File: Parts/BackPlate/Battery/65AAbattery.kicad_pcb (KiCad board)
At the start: 2 copper layers, 172.9 x 20 mm, 10 parts, among them J1 Conn_01x02, J2 Conn_01x01, J3 Conn_01x01, J4 Conn_01x01, SW1 SW_Push_SPDT

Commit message: 寸法更新とか
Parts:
- J1: footprint kbd_Parts:Battery_XH2.5_GL_rev -> kbd_Parts:Battery_XH2.5_GL_Connector
- moved C1 9.45 mm to (148.8, 30.0)
- moved J1 6.00 mm to (139.4, 30.3), turned to 180 degrees
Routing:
- net GND: track 131.9 -> 124.6 mm
- net Net-(BT1-Pad1): track 263.3 -> 257.8 mm
- net Bat+: track 21.9 -> 27.2 mm
- net Net-(D1-Pad1): track 45.1 -> 44.3 mm
- net Net-(BT2-Pad1): track 157.0 -> 156.2 mm
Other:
- board size 172.9 x 20 mm -> 172.9 x 19.4 mm

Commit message: 諸々修正
今度はちゃんと説明書きを書く
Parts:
- removed D2: D, kbd_Parts:Diode_SMD_Rev
- BT1, BT2: footprint kbd_Parts:Battery_AAA_GL -> Battery:BatteryHolder_Keystone_2466_1xAAA
- moved C1 6.82 mm to (154.8, 33.3)
- moved D1 4.16 mm to (154.8, 26.2)
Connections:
- BT1 pad 2: GND -> Net-(BT1-Pad2)
- BT2 pad 1: Net-(BT2-Pad1) -> Net-(BT1-Pad2)
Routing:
- net Net-(BT2-Pad1): track 156.2 -> 0.00 mm
- net GND: track 124.6 -> 103.6 mm
- net Net-(BT1-Pad2): track 0.00 -> 14.7 mm
- net Bat+: track 27.2 -> 39.4 mm
- net Net-(D1-Pad1): track 44.3 -> 52.9 mm
- net Net-(BT1-Pad1): track 257.8 -> 266.4 mm
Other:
- board size 172.9 x 19.4 mm -> 171.9 x 19.4 mm

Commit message: ケース修正に伴う修正
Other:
- board size 171.9 x 19.4 mm -> 171.4 x 19.4 mm

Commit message: パーツ類大整理
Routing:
- net Net-(BT1-Pad2): track 14.7 -> 15.6 mm

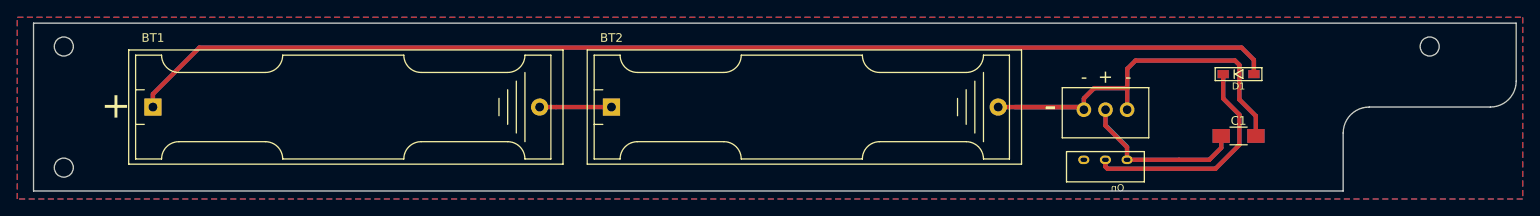
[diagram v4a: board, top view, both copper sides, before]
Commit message: 電池プレートの修正
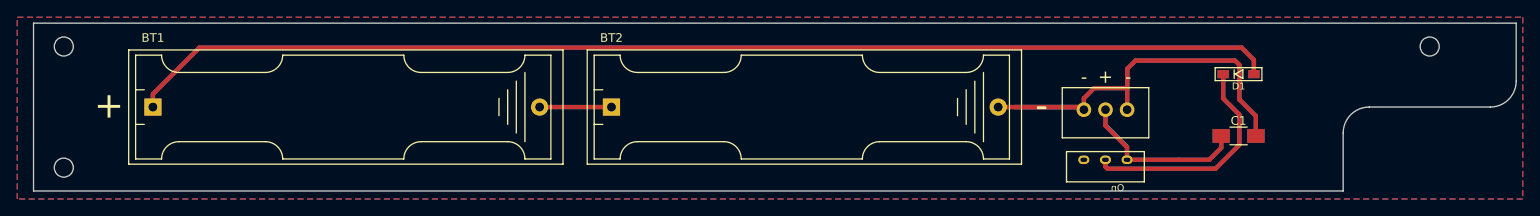
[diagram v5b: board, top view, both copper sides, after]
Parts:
- BT1, BT2: footprint Battery:BatteryHolder_Keystone_2466_1xAAA -> kbd_Parts:BatteryHolder_GL516_1xAAA
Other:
- board text added: "BT1"
- board text added: "BT2"
